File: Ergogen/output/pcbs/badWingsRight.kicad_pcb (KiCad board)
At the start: 2 copper layers, 149.9 x 112 mm, 152 parts

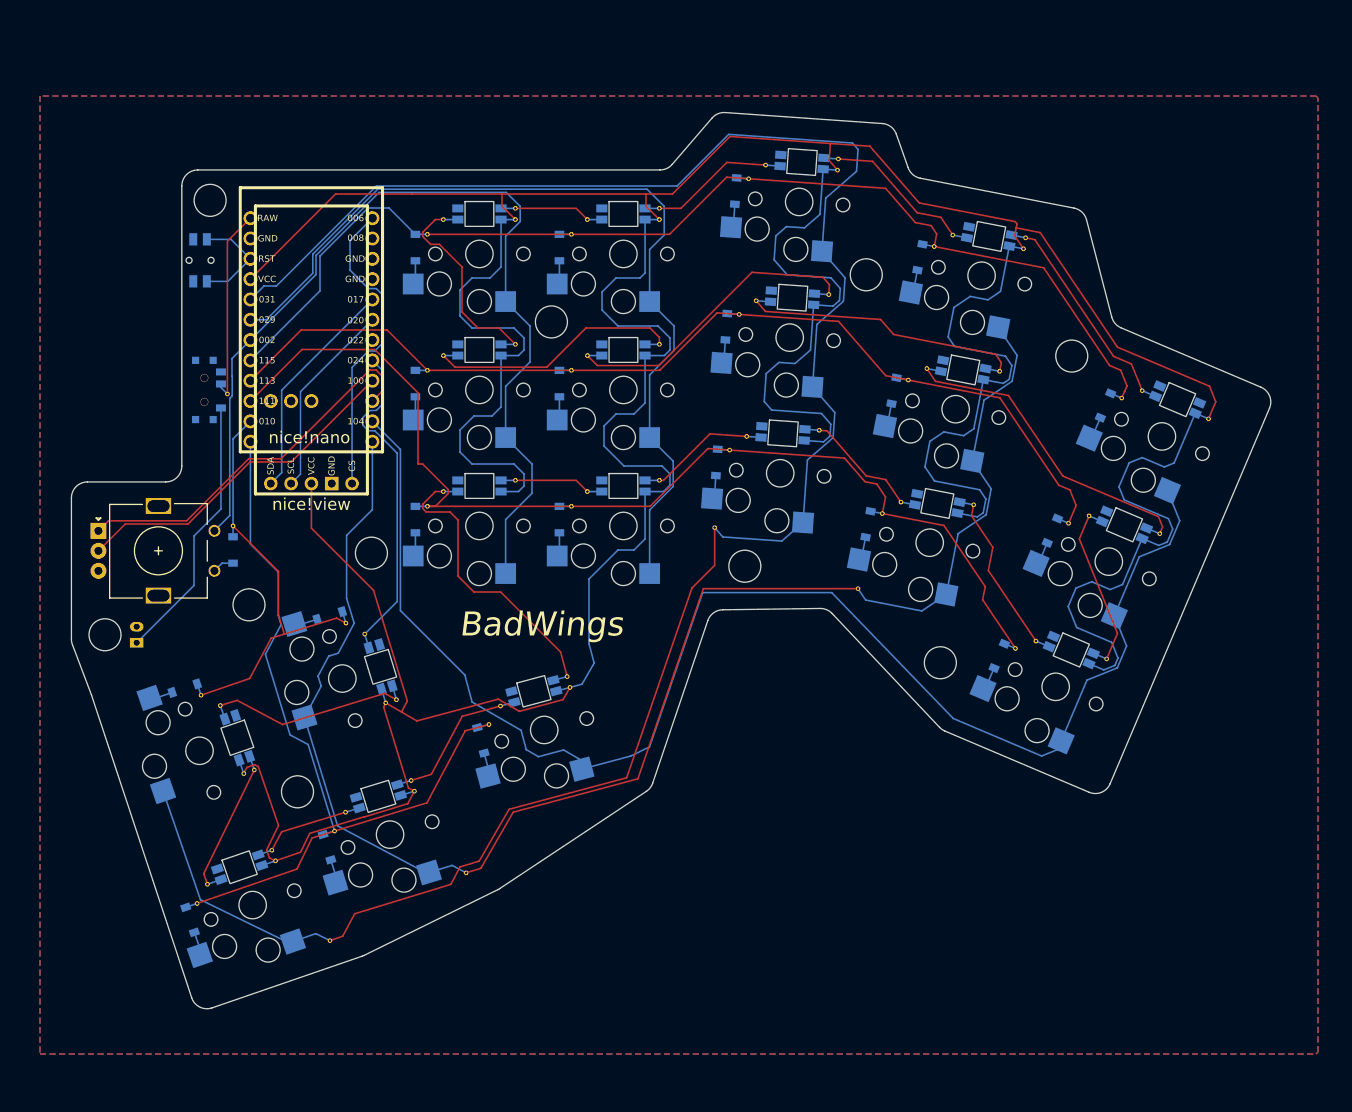
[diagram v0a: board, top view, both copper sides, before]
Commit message: Board v1.1 Complete
Complete prior to assembly
Case modifications could still be required
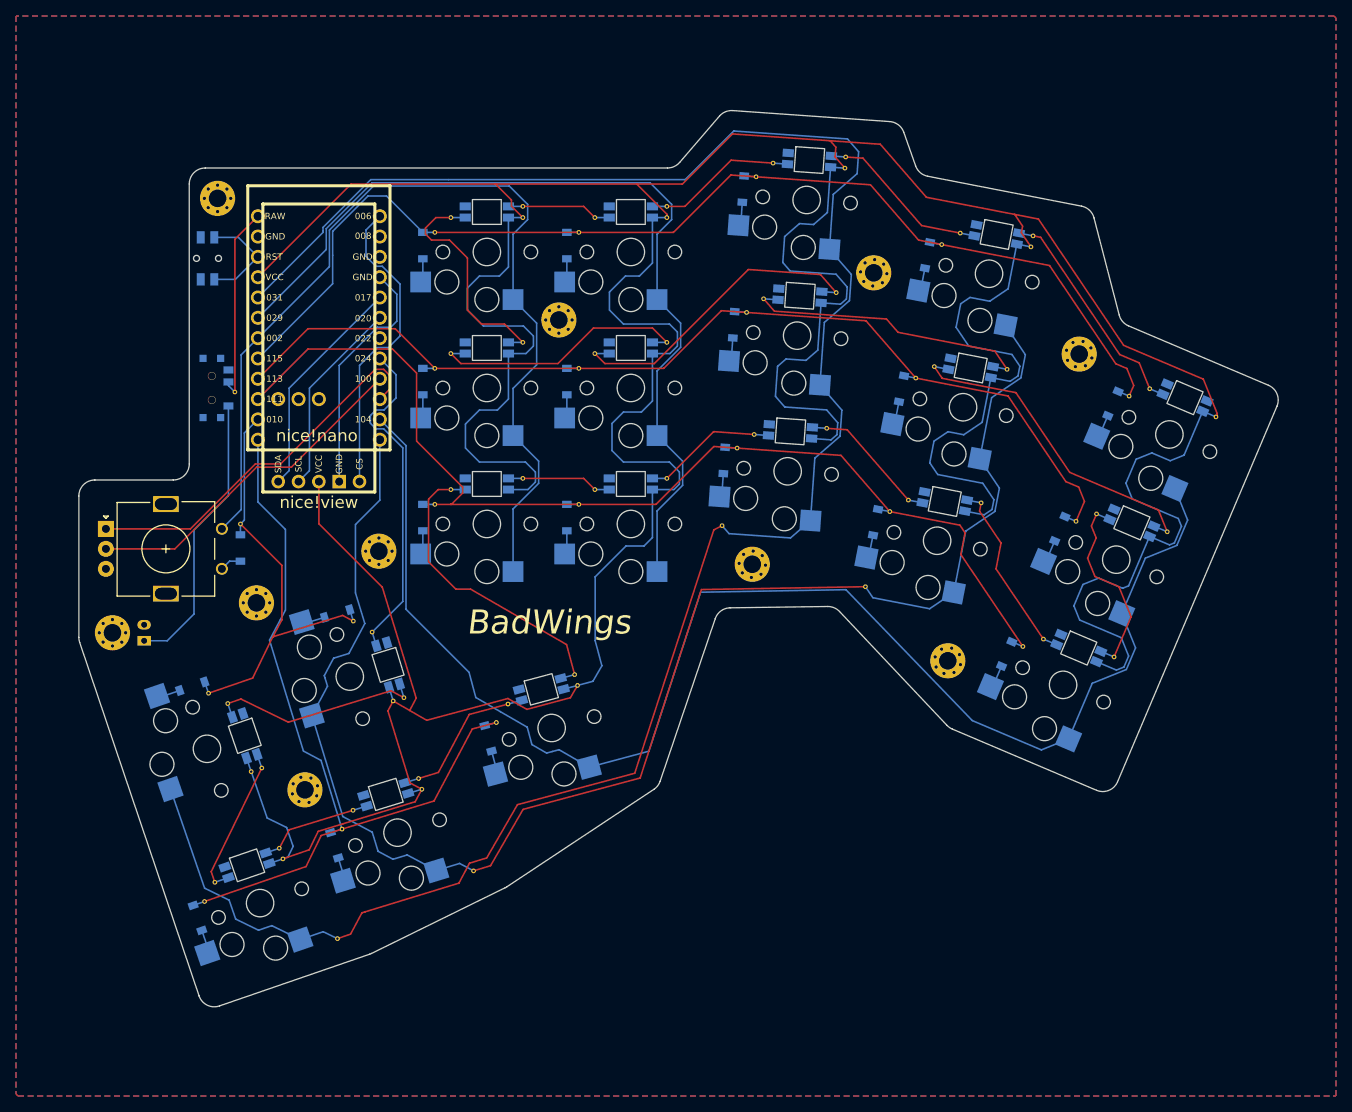
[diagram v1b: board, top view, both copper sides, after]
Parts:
- removed ? (x10): , HOLE_M2_TH
- removed the REF** at (291.8, 120.6)
- removed the REF** at (280.7, 141.3)
- removed the REF** at (227.4, 164.0)
- removed the REF** at (301.8, 135.1)
- removed the REF** at (253.7, 125.7)
- removed the REF** at (271.7, 159.7)
- removed the REF** at (317.4, 127.6)
- removed the REF** at (291.6, 152.8)
- removed the REF** at (287.6, 164.2)
- removed the REF** at (251.7, 161.5)
- removed the REF** at (326.2, 129.3)
- removed the REF** at (310.9, 161.0)
- removed the REF** at (294.0, 118.9)
- removed the REF** at (262.7, 125.7)
- removed the REF** at (228.7, 194.9)
- removed the REF** at (303.0, 118.1)
- removed the REF** at (336.6, 180.6)
- removed the REF** at (314.1, 144.3)
- removed the REF** at (308.5, 162.4)
- removed the REF** at (251.7, 144.5)
- removed the REF** at (269.1, 182.8)
- removed the REF** at (251.7, 127.5)
- removed the REF** at (253.7, 142.7)
- removed the REF** at (315.0, 129.1)
- removed the REF** at (327.7, 178.4)
- removed the REF** at (300.7, 152.0)
- removed the REF** at (290.6, 137.6)
- removed the REF** at (271.7, 125.7)
- removed the REF** at (269.7, 144.5)
- removed the REF** at (311.8, 145.8)
- removed the REF** at (302.9, 119.5)
- removed the REF** at (241.5, 176.1)
- removed the REF** at (256.5, 207.4)
- removed the REF** at (326.5, 128.0)
- removed the REF** at (280.7, 124.3)
- removed the REF** at (338.5, 148.0)
- removed the REF** at (259.4, 188.8)
- removed the REF** at (341.0, 147.1)
- removed the REF** at (250.1, 197.1)
- removed the REF** at (232.2, 204.5)
- removed the REF** at (226.7, 147.5)
- removed the REF** at (223.4, 185.2)
- removed the REF** at (253.7, 159.7)
- removed the REF** at (239.5, 215.8)
- removed the REF** at (230.0, 194.5)
- removed the REF** at (243.8, 177.5)
- removed the REF** at (269.5, 184.2)
- removed the REF** at (331.8, 163.7)
- removed the REF** at (262.7, 141.3)
- removed the REF** at (325.2, 179.3)
- removed the REF** at (289.5, 154.5)
- removed the REF** at (280.7, 125.7)
- removed the REF** at (280.7, 158.3)
- removed the REF** at (334.4, 162.7)
- removed the REF** at (260.8, 186.5)
- removed the REF** at (262.7, 158.3)
- removed the REF** at (323.2, 144.7)
- removed the REF** at (343.2, 165.0)
- removed the REF** at (349.3, 150.6)
- removed the REF** at (320.0, 161.4)
- removed the REF** at (240.1, 202.1)
- removed the REF** at (269.7, 161.5)
- removed the REF** at (292.8, 135.8)
- removed the REF** at (271.7, 142.7)
- removed the REF** at (224.2, 208.8)
- removed the REF** at (247.8, 185.7)
- removed the REF** at (246.5, 186.1)
- removed the REF** at (305.5, 171.8)
- removed the REF** at (249.6, 195.8)
- removed the REF** at (269.7, 127.5)
- removed the REF** at (241.4, 199.8)
- removed the REF** at (262.7, 124.3)
- removed the REF** at (222.9, 211.2)
- removed the REF** at (225.8, 186.4)
- removed the REF** at (232.7, 205.9)
- added REF**: VIA-0.6mm, VIA-0.6mm, F.Cu at (270.6, 161.3)
- added REF**: VIA-0.6mm, VIA-0.6mm, F.Cu at (281.6, 124.0)
- added REF**: VIA-0.6mm, VIA-0.6mm, F.Cu at (254.6, 125.4)
- added REF**: VIA-0.6mm, VIA-0.6mm, F.Cu at (241.0, 201.9)
- added REF**: VIA-0.6mm, VIA-0.6mm, F.Cu at (233.2, 204.3)
- added REF**: VIA-0.6mm, VIA-0.6mm, F.Cu at (311.8, 160.8)
- added REF**: VIA-0.6mm, VIA-0.6mm, F.Cu at (225.1, 208.5)
- added REF**: VIA-0.6mm, VIA-0.6mm, F.Cu at (339.4, 147.8)
- added REF**: VIA-0.6mm, VIA-0.6mm, F.Cu at (301.6, 151.8)
- added REF**: VIA-0.6mm, VIA-0.6mm, F.Cu at (242.4, 199.5)
- added REF**: VIA-0.6mm, VIA-0.6mm, F.Cu at (257.4, 207.1)
- added REF**: VIA-0.6mm, VIA-0.6mm, F.Cu at (228.3, 163.7)
- added REF**: VIA-0.6mm, VIA-0.6mm, F.Cu at (303.9, 119.3)
- added REF**: VIA-0.6mm, VIA-0.6mm, F.Cu at (342.0, 146.8)
- added REF**: VIA-0.6mm, VIA-0.6mm, F.Cu at (318.3, 127.4)
- added REF**: VIA-0.6mm, VIA-0.6mm, F.Cu at (260.3, 188.6)
- added REF**: VIA-0.6mm, VIA-0.6mm, F.Cu at (281.6, 158.0)
- added REF**: VIA-0.6mm, VIA-0.6mm, F.Cu at (291.6, 137.3)
- added REF**: VIA-0.6mm, VIA-0.6mm, F.Cu at (272.6, 125.4)
- added REF**: VIA-0.6mm, VIA-0.6mm, F.Cu at (337.5, 180.4)
- added REF**: VIA-0.6mm, VIA-0.6mm, F.Cu at (263.6, 125.4)
- added REF**: VIA-0.6mm, VIA-0.6mm, F.Cu at (288.5, 164.0)
- added REF**: VIA-0.6mm, VIA-0.6mm, F.Cu at (350.2, 150.4)
- added REF**: VIA-0.6mm, VIA-0.6mm, F.Cu at (270.1, 182.6)
- added REF**: VIA-0.6mm, VIA-0.6mm, F.Cu at (261.7, 186.3)
- added REF**: VIA-0.6mm, VIA-0.6mm, F.Cu at (263.6, 141.0)
- added REF**: VIA-0.6mm, VIA-0.6mm, F.Cu at (270.6, 127.3)
- added REF**: VIA-0.6mm, VIA-0.6mm, F.Cu at (302.8, 134.8)
- added REF**: VIA-0.6mm, VIA-0.6mm, F.Cu at (327.1, 129.1)
- added REF**: VIA-0.6mm, VIA-0.6mm, F.Cu at (223.8, 210.9)
- added REF**: VIA-0.6mm, VIA-0.6mm, F.Cu at (272.6, 142.4)
- added REF**: VIA-0.6mm, VIA-0.6mm, F.Cu at (344.2, 164.7)
- added REF**: VIA-0.6mm, VIA-0.6mm, F.Cu at (294.9, 118.6)
- added REF**: VIA-0.6mm, VIA-0.6mm, F.Cu at (240.4, 215.6)
- added REF**: VIA-0.6mm, VIA-0.6mm, F.Cu at (320.9, 161.1)
- added REF**: VIA-0.6mm, VIA-0.6mm, F.Cu at (270.4, 183.9)
- added REF**: VIA-0.6mm, VIA-0.6mm, F.Cu at (270.6, 144.3)
- added REF**: VIA-0.6mm, VIA-0.6mm, F.Cu at (251.0, 196.9)
- added REF**: VIA-0.6mm, VIA-0.6mm, F.Cu at (247.4, 185.9)
- added REF**: VIA-0.6mm, VIA-0.6mm, F.Cu at (292.5, 152.6)
- added REF**: VIA-0.6mm, VIA-0.6mm, F.Cu at (306.4, 171.6)
- added REF**: VIA-0.6mm, VIA-0.6mm, F.Cu at (292.8, 120.3)
- added REF**: VIA-0.6mm, VIA-0.6mm, F.Cu at (327.4, 127.7)
- added REF**: VIA-0.6mm, VIA-0.6mm, F.Cu at (309.5, 162.2)
- added REF**: VIA-0.6mm, VIA-0.6mm, F.Cu at (233.6, 205.6)
- added REF**: VIA-0.6mm, VIA-0.6mm, F.Cu at (229.7, 194.7)
- added REF**: VIA-0.6mm, VIA-0.6mm, F.Cu at (254.6, 142.4)
- added REF**: VIA-0.6mm, VIA-0.6mm, F.Cu at (252.6, 161.3)
- added REF**: VIA-0.6mm, VIA-0.6mm, F.Cu at (281.6, 141.0)
- added REF**: VIA-0.6mm, VIA-0.6mm, F.Cu at (326.1, 179.1)
- added REF**: VIA-0.6mm, VIA-0.6mm, F.Cu at (324.1, 144.4)
- added REF**: VIA-0.6mm, VIA-0.6mm, F.Cu at (290.4, 154.3)
- added REF**: VIA-0.6mm, VIA-0.6mm, F.Cu at (254.6, 159.4)
- added REF**: VIA-0.6mm, VIA-0.6mm, F.Cu at (293.7, 135.6)
- added REF**: VIA-0.6mm, VIA-0.6mm, F.Cu at (304.0, 117.9)
- added REF**: VIA-0.6mm, VIA-0.6mm, F.Cu at (248.7, 185.5)
- added REF**: VIA-0.6mm, VIA-0.6mm, F.Cu at (335.3, 162.5)
- added REF**: VIA-0.6mm, VIA-0.6mm, F.Cu at (312.7, 145.5)
- added REF**: VIA-0.6mm, VIA-0.6mm, F.Cu at (263.6, 158.0)
- added REF**: VIA-0.6mm, VIA-0.6mm, F.Cu at (226.7, 186.2)
- added REF**: VIA-0.6mm, VIA-0.6mm, F.Cu at (252.6, 127.3)
- added REF**: VIA-0.6mm, VIA-0.6mm, F.Cu at (332.8, 163.4)
- added REF**: VIA-0.6mm, VIA-0.6mm, F.Cu at (316.0, 128.8)
- added REF**: VIA-0.6mm, VIA-0.6mm, F.Cu at (272.6, 159.4)
- added REF**: VIA-0.6mm, VIA-0.6mm, F.Cu at (281.6, 125.4)
- added REF**: VIA-0.6mm, VIA-0.6mm, F.Cu at (315.0, 144.1)
- added REF**: VIA-0.6mm, VIA-0.6mm, F.Cu at (242.4, 175.9)
- added REF**: VIA-0.6mm, VIA-0.6mm, F.Cu at (244.8, 177.3)
- added REF**: VIA-0.6mm, VIA-0.6mm, F.Cu at (252.6, 144.3)
- added REF**: VIA-0.6mm, VIA-0.6mm, F.Cu at (250.6, 195.6)
- added REF**: VIA-0.6mm, VIA-0.6mm, F.Cu at (263.6, 124.0)
- added REF**: VIA-0.6mm, VIA-0.6mm, F.Cu at (328.7, 178.1)
- added REF**: VIA-0.6mm, VIA-0.6mm, F.Cu at (224.3, 184.9)
- added REF**: VIA-0.6mm, VIA-0.6mm, F.Cu at (227.6, 147.2)
- added REF**: VIA-0.6mm, VIA-0.6mm, F.Cu at (231.0, 194.2)
- added _76: , MountingHole_2.2mm_M2_Pad_Via, F.Cu at (236.4, 197.0)
- added _77: , MountingHole_2.2mm_M2_Pad_Via, F.Cu at (316.7, 180.8)
- added _78: , MountingHole_2.2mm_M2_Pad_Via, F.Cu at (333.2, 142.5)
- added _79: , MountingHole_2.2mm_M2_Pad_Via, F.Cu at (268.1, 138.2)
- added _80: , MountingHole_2.2mm_M2_Pad_Via, F.Cu at (212.3, 177.3)
- added _81: , MountingHole_2.2mm_M2_Pad_Via, F.Cu at (292.3, 168.8)
- added _82: , MountingHole_2.2mm_M2_Pad_Via, F.Cu at (307.5, 132.4)
- added _83: , MountingHole_2.2mm_M2_Pad_Via, F.Cu at (245.6, 167.1)
- added _84: , MountingHole_2.2mm_M2_Pad_Via, F.Cu at (230.3, 173.6)
- added _85: , MountingHole_2.2mm_M2_Pad_Via, F.Cu at (225.4, 123.0)
- moved LED19 0.96 mm to (229.1, 206.4)
- moved S14 0.96 mm to (259.1, 146.7)
- moved LED8 0.96 mm to (298.2, 135.2)
- moved S15 0.96 mm to (259.1, 129.7)
- moved D9 0.96 mm to (291.2, 121.9)
- moved T1 0.96 mm to (224.7, 146.7)
- moved S18 0.96 mm to (242.0, 182.8)
- moved LED14 0.96 mm to (259.1, 141.7)
- moved LED18 0.96 mm to (246.8, 181.4)
- moved D15 0.96 mm to (251.1, 128.9)
- moved ROT1 0.96 mm to (219.1, 166.9)
- moved LED7 0.96 mm to (297.1, 152.2)
- moved D21 0.96 mm to (228.3, 166.7)
- moved D11 0.96 mm to (269.1, 145.9)
- moved LED11 0.96 mm to (277.1, 141.7)
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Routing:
- net GND: track 0.00 -> 30.4 mm
- net VCC: track 612.2 -> 618.3 mm
- net LED10: track 22.9 -> 24.8 mm
- net LED15: track 27.9 -> 29.7 mm
- net pos: track 33.7 -> 35.4 mm
- net P002: track 121.1 -> 122.7 mm
- net P031: track 262.6 -> 261.1 mm
- net P106: track 192.7 -> 194.1 mm
- net P111: track 141.8 -> 140.5 mm
- net P115: track 144.7 -> 145.6 mm
- net LED14: track 34.6 -> 33.7 mm
- net P010: track 56.3 -> 57.1 mm
- net P024: track 41.8 -> 42.6 mm
- net P029: track 112.4 -> 113.1 mm
- net LED13: track 40.9 -> 40.2 mm
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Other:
- outline, holes or cut-outs redrawn
